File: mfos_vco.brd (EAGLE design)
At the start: 100 x 81.5 mm, 60 parts, among them IC1 TL072P, IC2 TL072P, IC3 TL072P, T1 2N3904, T2 2N3904, U1 POWER, U2 2N5457

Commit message: same problem
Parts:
- D1: device SparkFun-DiscreteSemi:DIODE-1N4148 -> SparkFun-DiscreteSemi:DIODE-1N4001
- R14: value 100k -> 20k
- moved LINEAR 82.0 mm to (76.8, -0.64), turned to 180 degrees
- moved SYNC 81.4 mm to (64.1, -0.64), turned to 180 degrees
- moved CV1 80.9 mm to (12.7, -0.81), turned to 180 degrees
- moved RAMP 80.7 mm to (89.5, -0.64), turned to 180 degrees
- moved FINE 74.6 mm to (42.5, 3.30), turned to 0 degrees
- moved COARSE 74.6 mm to (24.1, 3.30), turned to 0 degrees
- moved R1 63.9 mm to (37.5, 10.8), turned to 270 degrees
- moved R4 61.8 mm to (47.6, 10.8), turned to 90 degrees
- moved R6 61.7 mm to (19.1, 10.8), turned to 270 degrees
- moved R5 61.6 mm to (29.2, 10.8), turned to 90 degrees
- moved R8 59.2 mm to (24.3, 10.8), turned to 90 degrees
- moved R7 59.1 mm to (42.5, 10.8), turned to 90 degrees
- moved R10 50.2 mm to (17.1, 18.4)
- moved CV2 45.6 mm to (9.53, 21.0)
- moved R17 45.3 mm to (33.7, 24.0), turned to 90 degrees
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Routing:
- net -12V: track 233.9 -> 163.1 mm, vias 2 -> 6
- net GND: track 274.4 -> 341.2 mm, vias 4 -> 2
- net N$20: track 13.1 -> 54.1 mm
- net N$11: track 23.2 -> 53.0 mm
- net N$35: track 44.2 -> 20.5 mm
- net N$31: track 32.8 -> 9.93 mm
- net +12V: track 277.0 -> 256.3 mm, vias 2 -> 0
- net N$36: track 5.33 -> 25.2 mm
- net N$33: track 29.2 -> 9.42 mm
- net N$32: track 9.55 -> 28.9 mm
- net N$9: track 33.9 -> 17.1 mm
- net N$22: track 42.6 -> 27.9 mm, vias 0 -> 2
- net N$16: track 15.2 -> 28.5 mm
- net N$25: track 6.50 -> 19.7 mm
- net N$29: track 3.18 -> 11.8 mm
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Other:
- board size 100 x 81.5 mm -> 100.8 x 80.8 mm

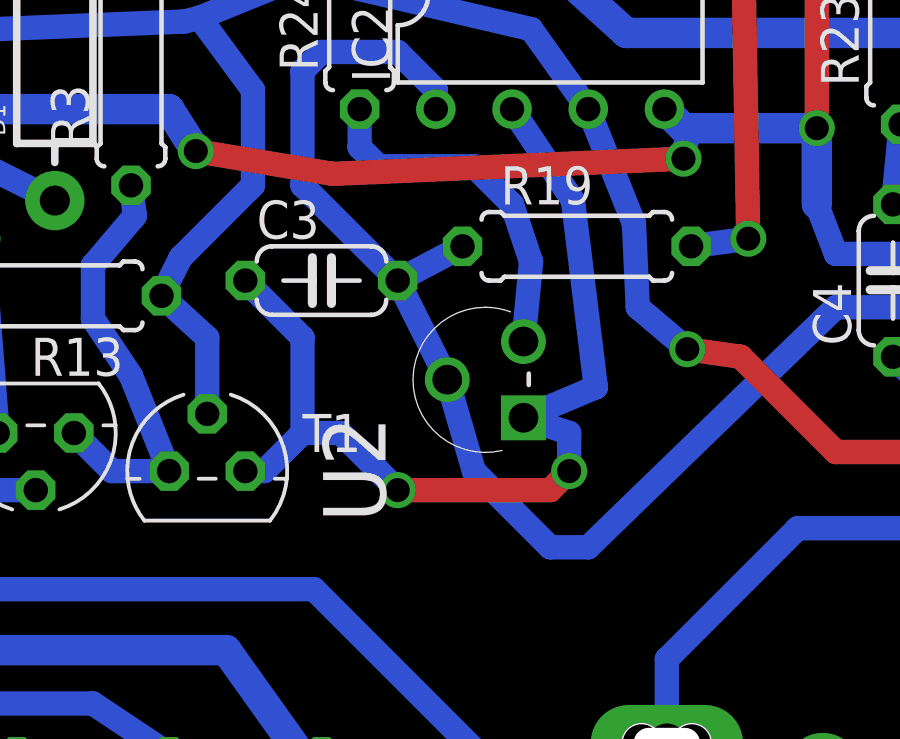
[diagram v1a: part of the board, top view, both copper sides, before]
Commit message: changed to mpf102 device to ensure pinout
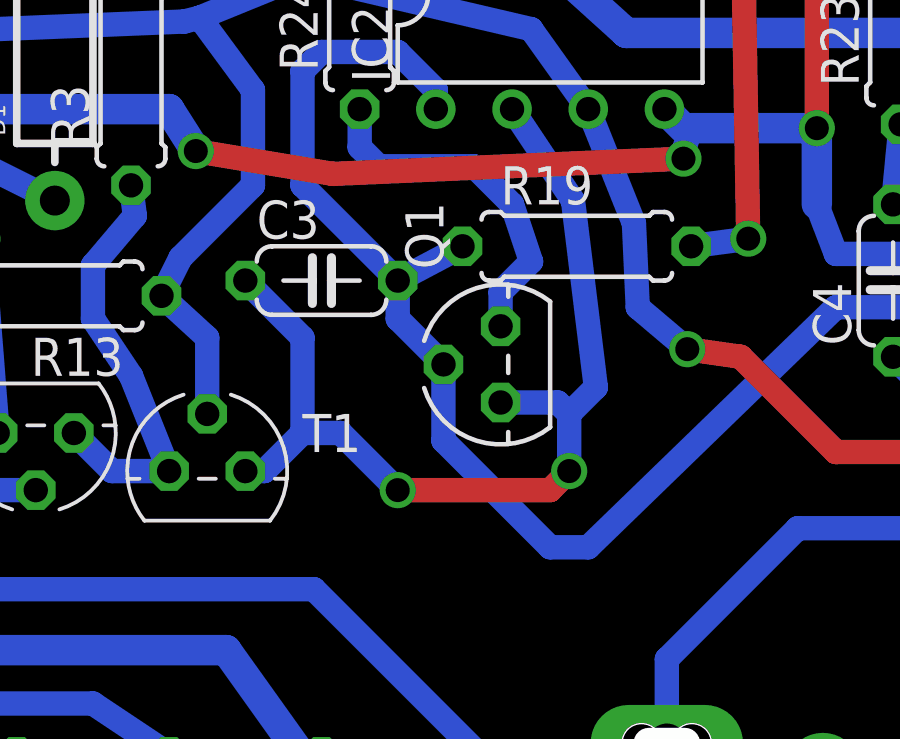
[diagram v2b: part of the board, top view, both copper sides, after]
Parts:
- removed U2: 2N5457, Fairchild_By_element14_Batch_1:TO127P254X732-3
- added Q1: MPF102, bt_transistor:TO92F
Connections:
- net N$21: now also Q1.2; no longer U2.2
- net N$23: now also Q1.1; no longer U2.1
- net N$29: now also Q1.3; no longer U2.3
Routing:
- net N$21: track 45.5 -> 46.1 mm
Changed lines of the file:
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@@
 <layer number="223" name="223bmp" color="24" fill="1" visible="no" active="no"/>
 <layer number="224" name="224bmp" color="25" fill="1" visible="no" active="no"/>
+<layer number="231" name="Eagle3D_PG1" color="14" fill="1" visible="yes" active="yes"/>
+<layer number="232" name="Eagle3D_PG2" color="14" fill="2" visible="yes" active="yes"/>
+<layer number="233" name="Eagle3D_PG3" color="14" fill="4" visible="yes" active="yes"/>
 <layer number="250" name="Descript" color="3" fill="1" visible="no" active="no"/>
 <layer number="251" name="SMDround" color="12" fill="11" visible="no" active="no"/>
@@
 <element name="TEMPCO" library="rcl" package="0207/2V" value="2k" x="24.765" y="30.48"/>
 <element name="U1" library="eurorack" package="POWER_16" value="POWER" x="8.255" y="40.005" rot="R90"/>
-<element name="U2" library="Fairchild_By_element14_Batch_1" package="TO127P254X732-3" value="2N5457" x="51.816" y="28.448" rot="R90">
-<attribute name="PACKAGE" value="TO-92" x="51.816" y="28.448" size="1.778" layer="27" rot="R90" display="off"/>
-<attribute name="OC_NEWARK" value="58K2809" x="51.816" y="28.448" size="1.778" layer="27" rot="R90" display="off"/>
-<attribute name="MPN" value="2N5457" x="51.816" y="28.448" size="1.778" layer="27" rot="R90" display="off"/>
-<attribute name="SUPPLIER" value="Fairchild" x="51.816" y="28.448" size="1.778" layer="27" rot="R90" display="off"/>
-<attribute name="OC_FARNELL" value="1653694" x="51.816" y="28.448" size="1.778" layer="27" rot="R90" display="off"/>
-</element>
+<element name="Q1" library="bt_transistor" package="TO92F" value="MPF102" x="53.594" y="27.686" rot="R90"/>
 </elements>
 <signals>
@@
 <contactref element="R19" pad="1"/>
 <contactref element="C3" pad="2"/>
-<contactref element="U2" pad="2"/>
 <contactref element="R28" pad="1"/>
 <wire x1="69.85" y1="27.94" x2="67.945" y2="29.591" width="0.8128" layer="16"/>
@@
 <wire x1="64.77" y1="29.591" x2="56.515" y2="21.59" width="0.8128" layer="16"/>
 <wire x1="56.515" y1="21.59" x2="55.245" y2="21.59" width="0.8128" layer="16"/>
-<wire x1="55.245" y1="21.59" x2="52.705" y2="24.13" width="0.8128" layer="16"/>
-<wire x1="52.705" y1="24.13" x2="51.816" y2="27.178" width="0.8128" layer="16"/>
-<wire x1="51.816" y1="27.178" x2="50.165" y2="30.48" width="0.8128" layer="16"/>
+<wire x1="55.245" y1="21.59" x2="51.689" y2="25.146" width="0.8128" layer="16"/>
 <wire x1="50.165" y1="30.48" x2="52.324" y2="31.623" width="0.8128" layer="16"/>
 <wire x1="51.435" y1="36.195" x2="51.435" y2="36.83" width="0.8128" layer="16"/>
@@
 <wire x1="46.99" y1="37.465" x2="46.99" y2="33.655" width="0.8128" layer="16"/>
 <wire x1="46.99" y1="33.655" x2="50.165" y2="30.48" width="0.8128" layer="16"/>
+<contactref element="Q1" pad="2"/>
+<wire x1="51.689" y1="27.686" x2="51.689" y2="25.146" width="0.8128" layer="16"/>
+<wire x1="50.165" y1="30.48" x2="50.165" y2="29.21" width="0.8128" layer="16"/>
+<wire x1="50.165" y1="29.21" x2="51.689" y2="27.686" width="0.8128" layer="16"/>
 </signal>
 <signal name="N$22">
@@
 <contactref element="T1" pad="1"/>
 <contactref element="IC2" pad="2"/>
-<contactref element="U2" pad="1"/>
 <contactref element="C3" pad="1"/>
 <wire x1="45.085" y1="24.13" x2="45.72" y2="24.13" width="0.8128" layer="16"/>
@@
 <wire x1="46.99" y1="25.4" x2="46.99" y2="28.575" width="0.8128" layer="16"/>
 <wire x1="46.99" y1="28.575" x2="45.085" y2="30.48" width="0.8128" layer="16"/>
-<wire x1="54.356" y1="25.908" x2="56.769" y2="26.924" width="0.8128" layer="16"/>
 <wire x1="56.769" y1="26.924" x2="56.007" y2="33.147" width="0.8128" layer="16"/>
 <wire x1="56.007" y1="33.147" x2="53.975" y2="36.195" width="0.8128" layer="16"/>
@@
 <wire x1="55.245" y1="23.495" x2="55.88" y2="24.13" width="0.8128" layer="1"/>
 <via x="55.88" y="24.13" extent="1-16" drill="0.8" shape="square"/>
-<wire x1="55.88" y1="24.13" x2="55.88" y2="25.4" width="0.8128" layer="16"/>
-<wire x1="55.88" y1="25.4" x2="54.356" y2="25.908" width="0.8128" layer="16"/>
+<wire x1="55.88" y1="24.13" x2="55.88" y2="26.035" width="0.8128" layer="16"/>
+<contactref element="Q1" pad="1"/>
+<wire x1="55.88" y1="26.035" x2="56.769" y2="26.924" width="0.8128" layer="16"/>
+<wire x1="53.594" y1="26.416" x2="55.499" y2="26.416" width="0.8128" layer="16"/>
+<wire x1="55.499" y1="26.416" x2="55.88" y2="26.035" width="0.8128" layer="16"/>
 </signal>
 <signal name="N$24">
@@
 </signal>
 <signal name="N$29">
-<contactref element="U2" pad="3"/>
 <contactref element="R24" pad="1"/>
-<wire x1="54.356" y1="28.448" x2="54.61" y2="31.115" width="0.8128" layer="16"/>
 <wire x1="54.61" y1="31.115" x2="53.975" y2="33.02" width="0.8128" layer="16"/>
 <wire x1="53.975" y1="33.02" x2="52.705" y2="34.29" width="0.8128" layer="16"/>
@@
 <wire x1="49.53" y1="34.29" x2="48.895" y2="34.925" width="0.8128" layer="16"/>
 <wire x1="48.895" y1="34.925" x2="48.895" y2="36.195" width="0.8128" layer="16"/>
+<contactref element="Q1" pad="3"/>
+<wire x1="53.594" y1="28.956" x2="53.594" y2="30.099" width="0.8128" layer="16"/>
+<wire x1="53.594" y1="30.099" x2="54.61" y2="31.115" width="0.8128" layer="16"/>
 </signal>
 <signal name="N$30">
